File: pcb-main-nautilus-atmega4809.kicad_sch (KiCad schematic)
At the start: 0 parts

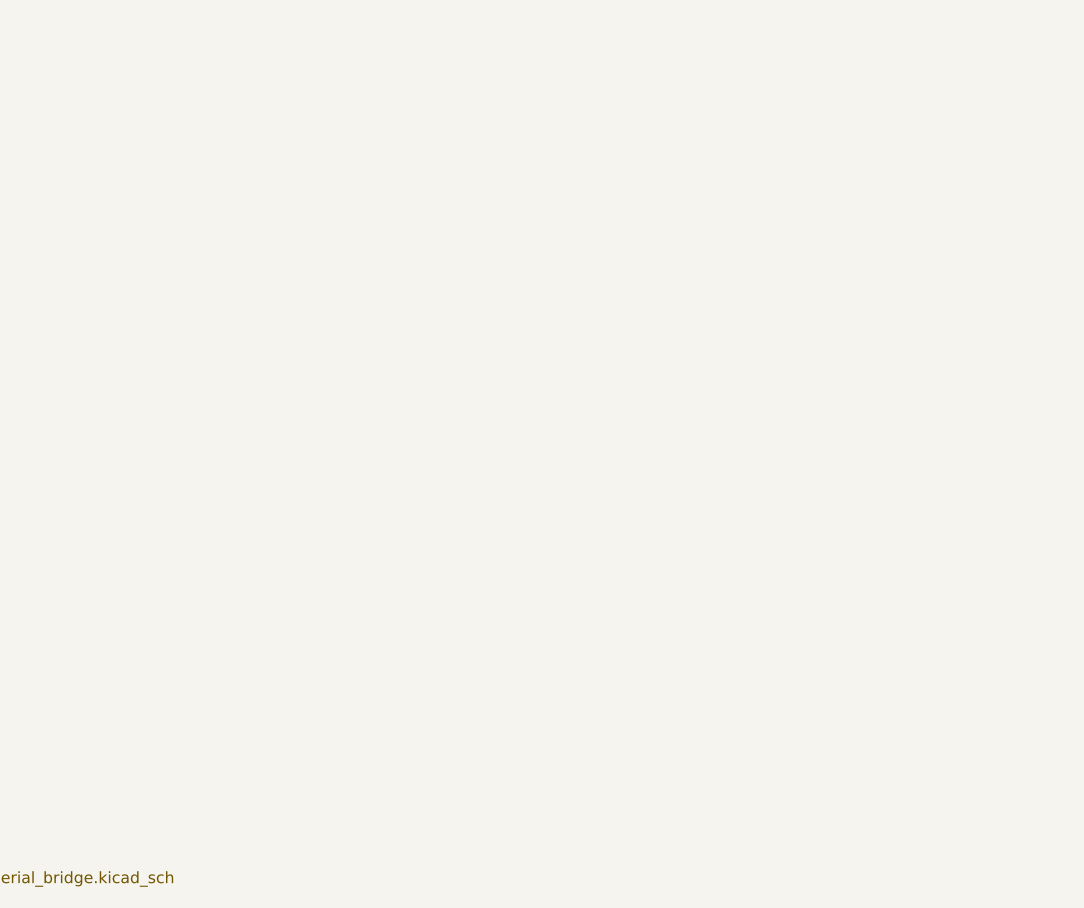
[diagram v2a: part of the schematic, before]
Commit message: Add bi-directional level shifter sheet
Supports #2.
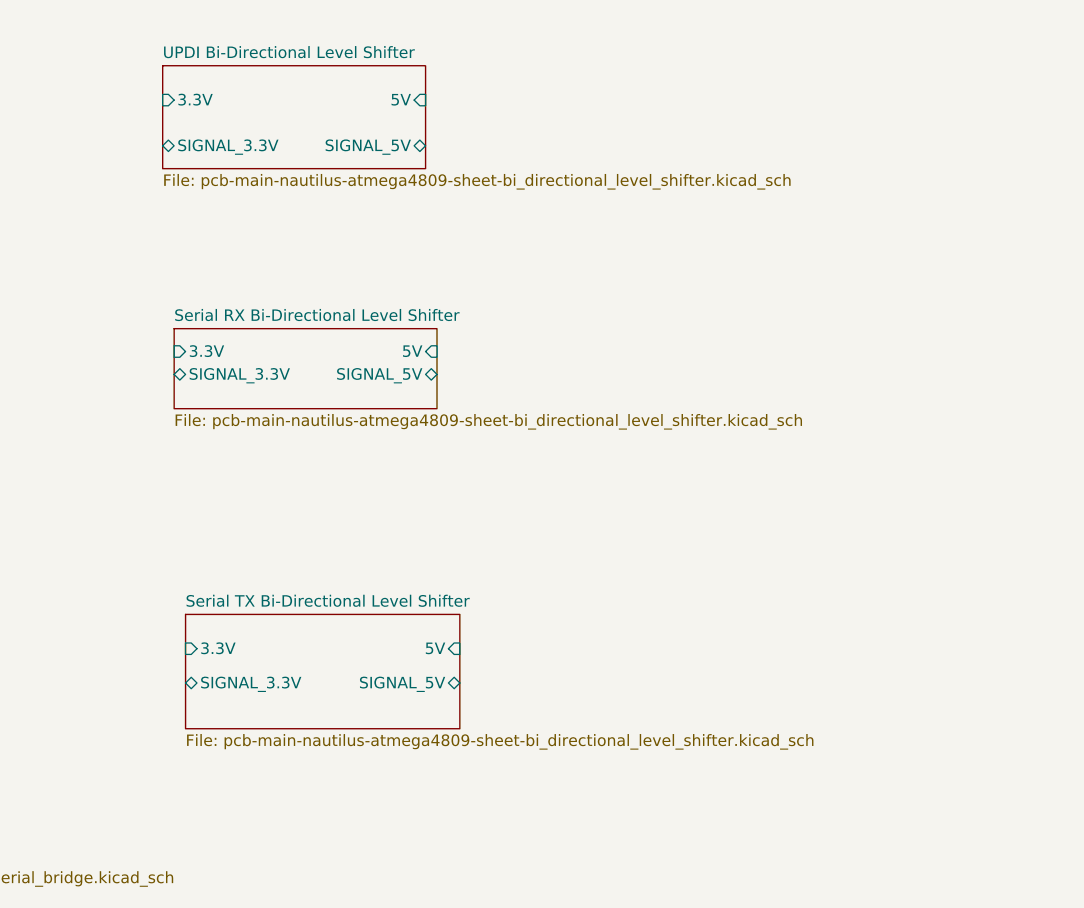
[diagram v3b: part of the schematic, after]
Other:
- added sheet Serial RX Bi-Directional Level Shifter (pcb-main-nautilus-atmega4809-sheet-bi_directional_level_shifter.kicad_sch)
- added sheet Serial TX Bi-Directional Level Shifter (pcb-main-nautilus-atmega4809-sheet-bi_directional_level_shifter.kicad_sch)
- added sheet UPDI Bi-Directional Level Shifter (pcb-main-nautilus-atmega4809-sheet-bi_directional_level_shifter.kicad_sch)
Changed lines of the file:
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@@
     (comment 1 "Derivative of the \"Arduino UNO Rev3\" (https://docs.arduino.cc/hardware/uno-rev3) and\\n\"Arduino Nano Every\" (https://docs.arduino.cc/hardware/nano-every) reference designs")
   )
+  (sheet (at 157.48 40.64) (size 29.21 11.43) (fields_autoplaced)
+    (stroke (width 0.1524) (type solid) (color 0 0 0 0))
+    (fill (color 0 0 0 0.0000))
+    (property "Sheet name" "UPDI Bi-Directional Level Shifter" (id 0) (at 157.48 39.9284 0)
+      (effects (font (size 1.27 1.27)) (justify left bottom))
+    )
+    (property "Sheet file" "pcb-main-nautilus-atmega4809-sheet-bi_directional_level_shifter.kicad_sch" (id 1) (at 157.48 52.6546 0)
+      (effects (font (size 1.27 1.27)) (justify left top))
+    )
+    (pin "5V" input (at 186.69 44.45 0)
+      (effects (font (size 1.27 1.27)) (justify right))
+    )
+    (pin "SIGNAL_5V" bidirectional (at 186.69 49.53 0)
+      (effects (font (size 1.27 1.27)) (justify right))
+    )
+    (pin "3.3V" input (at 157.48 44.45 180)
+      (effects (font (size 1.27 1.27)) (justify left))
+    )
+    (pin "SIGNAL_3.3V" bidirectional (at 157.48 49.53 180)
+      (effects (font (size 1.27 1.27)) (justify left))
+    )
+  )
   (sheet (at 76.2 38.1) (size 20.32 20.32) (fields_autoplaced)
     (stroke (width 0.1524) (type solid) (color 0 0 0 0))
@@
     (pin "UPDI" bidirectional (at 106.68 106.68 0)
       (effects (font (size 1.27 1.27)) (justify right))
+    )
+  )
+  (sheet (at 160.02 101.6) (size 30.48 12.7) (fields_autoplaced)
+    (stroke (width 0.1524) (type solid) (color 0 0 0 0))
+    (fill (color 0 0 0 0.0000))
+    (property "Sheet name" "Serial TX Bi-Directional Level Shifter" (id 0) (at 160.02 100.8884 0)
+      (effects (font (size 1.27 1.27)) (justify left bottom))
+    )
+    (property "Sheet file" "pcb-main-nautilus-atmega4809-sheet-bi_directional_level_shifter.kicad_sch" (id 1) (at 160.02 114.8846 0)
+      (effects (font (size 1.27 1.27)) (justify left top))
+    )
+    (pin "5V" input (at 190.5 105.41 0)
+      (effects (font (size 1.27 1.27)) (justify right))
+    )
+    (pin "SIGNAL_5V" bidirectional (at 190.5 109.22 0)
+      (effects (font (size 1.27 1.27)) (justify right))
+    )
+    (pin "3.3V" input (at 160.02 105.41 180)
+      (effects (font (size 1.27 1.27)) (justify left))
+    )
+    (pin "SIGNAL_3.3V" bidirectional (at 160.02 109.22 180)
+      (effects (font (size 1.27 1.27)) (justify left))
+    )
+  )
+  (sheet (at 158.75 69.85) (size 29.21 8.89) (fields_autoplaced)
+    (stroke (width 0.1524) (type solid) (color 0 0 0 0))
+    (fill (color 0 0 0 0.0000))
+    (property "Sheet name" "Serial RX Bi-Directional Level Shifter" (id 0) (at 158.75 69.1384 0)
+      (effects (font (size 1.27 1.27)) (justify left bottom))
+    )
+    (property "Sheet file" "pcb-main-nautilus-atmega4809-sheet-bi_directional_level_shifter.kicad_sch" (id 1) (at 158.75 79.3246 0)
+      (effects (font (size 1.27 1.27)) (justify left top))
+    )
+    (pin "5V" input (at 187.96 72.39 0)
+      (effects (font (size 1.27 1.27)) (justify right))
+    )
+    (pin "SIGNAL_5V" bidirectional (at 187.96 74.93 0)
+      (effects (font (size 1.27 1.27)) (justify right))
+    )
+    (pin "3.3V" input (at 158.75 72.39 180)
+      (effects (font (size 1.27 1.27)) (justify left))
+    )
+    (pin "SIGNAL_3.3V" bidirectional (at 158.75 74.93 180)
+      (effects (font (size 1.27 1.27)) (justify left))
     )
   )
@@
     (path "/5a33ba3c-72f7-420a-981d-98ac038c5559" (page "2"))
     (path "/9563730f-8d1a-4fdb-af84-834004e725da" (page "3"))
+    (path "/2696b8cf-0d11-49f9-8de6-4c9d32a16799" (page "4"))
+    (path "/b9953305-206e-463a-87bb-3c268da92256" (page "5"))
+    (path "/b67adff0-b650-44cc-9343-28972961f0fd" (page "6"))
   )
   (symbol_instances
@@
       (reference "NT1") (unit 1) (value "NetTie_3") (footprint "")
     )
+    (path "/2696b8cf-0d11-49f9-8de6-4c9d32a16799/faa0bcb3-92cf-49f0-8c93-d9591933f632"
+      (reference "Q1") (unit 1) (value "BSS138PW,115") (footprint "Package_TO_SOT_SMD:SOT-323_SC-70_Handsoldering")
+    )
+    (path "/b9953305-206e-463a-87bb-3c268da92256/faa0bcb3-92cf-49f0-8c93-d9591933f632"
+      (reference "Q2") (unit 1) (value "BSS138PW,115") (footprint "Package_TO_SOT_SMD:SOT-323_SC-70_Handsoldering")
+    )
+    (path "/b67adff0-b650-44cc-9343-28972961f0fd/faa0bcb3-92cf-49f0-8c93-d9591933f632"
+      (reference "Q3") (unit 1) (value "BSS138PW,115") (footprint "Package_TO_SOT_SMD:SOT-323_SC-70_Handsoldering")
+    )
     (path "/5a33ba3c-72f7-420a-981d-98ac038c5559/3e98dc00-be45-4498-ad45-de614d277a00"
       (reference "R1") (unit 1) (value "330/0.1W") (footprint "Resistor_SMD:R_0603_1608Metric_Pad0.98x0.95mm_HandSolder")
@@
       (reference "R4") (unit 1) (value "4.7k/0.1W") (footprint "Resistor_SMD:R_0603_1608Metric_Pad0.98x0.95mm_HandSolder")
     )
+    (path "/2696b8cf-0d11-49f9-8de6-4c9d32a16799/ac494291-0341-40e4-84fe-a220d54d9e87"
+      (reference "R5") (unit 1) (value "4.7k/0.1W") (footprint "Resistor_SMD:R_0603_1608Metric_Pad0.98x0.95mm_HandSolder")
+    )
+    (path "/2696b8cf-0d11-49f9-8de6-4c9d32a16799/08011bfc-ec9f-46b5-8bcb-363c7a858e08"
+      (reference "R6") (unit 1) (value "4.7k/0.1W") (footprint "Resistor_SMD:R_0603_1608Metric_Pad0.98x0.95mm_HandSolder")
+    )
+    (path "/b9953305-206e-463a-87bb-3c268da92256/ac494291-0341-40e4-84fe-a220d54d9e87"
+      (reference "R7") (unit 1) (value "4.7k/0.1W") (footprint "Resistor_SMD:R_0603_1608Metric_Pad0.98x0.95mm_HandSolder")
+    )
+    (path "/b9953305-206e-463a-87bb-3c268da92256/08011bfc-ec9f-46b5-8bcb-363c7a858e08"
+      (reference "R8") (unit 1) (value "4.7k/0.1W") (footprint "Resistor_SMD:R_0603_1608Metric_Pad0.98x0.95mm_HandSolder")
+    )
+    (path "/b67adff0-b650-44cc-9343-28972961f0fd/ac494291-0341-40e4-84fe-a220d54d9e87"
+      (reference "R9") (unit 1) (value "4.7k/0.1W") (footprint "Resistor_SMD:R_0603_1608Metric_Pad0.98x0.95mm_HandSolder")
+    )
+    (path "/b67adff0-b650-44cc-9343-28972961f0fd/08011bfc-ec9f-46b5-8bcb-363c7a858e08"
+      (reference "R10") (unit 1) (value "4.7k/0.1W") (footprint "Resistor_SMD:R_0603_1608Metric_Pad0.98x0.95mm_HandSolder")
+    )
     (path "/5a33ba3c-72f7-420a-981d-98ac038c5559/678f9d4d-d6a2-4e0c-8b54-d5be33abe55a"

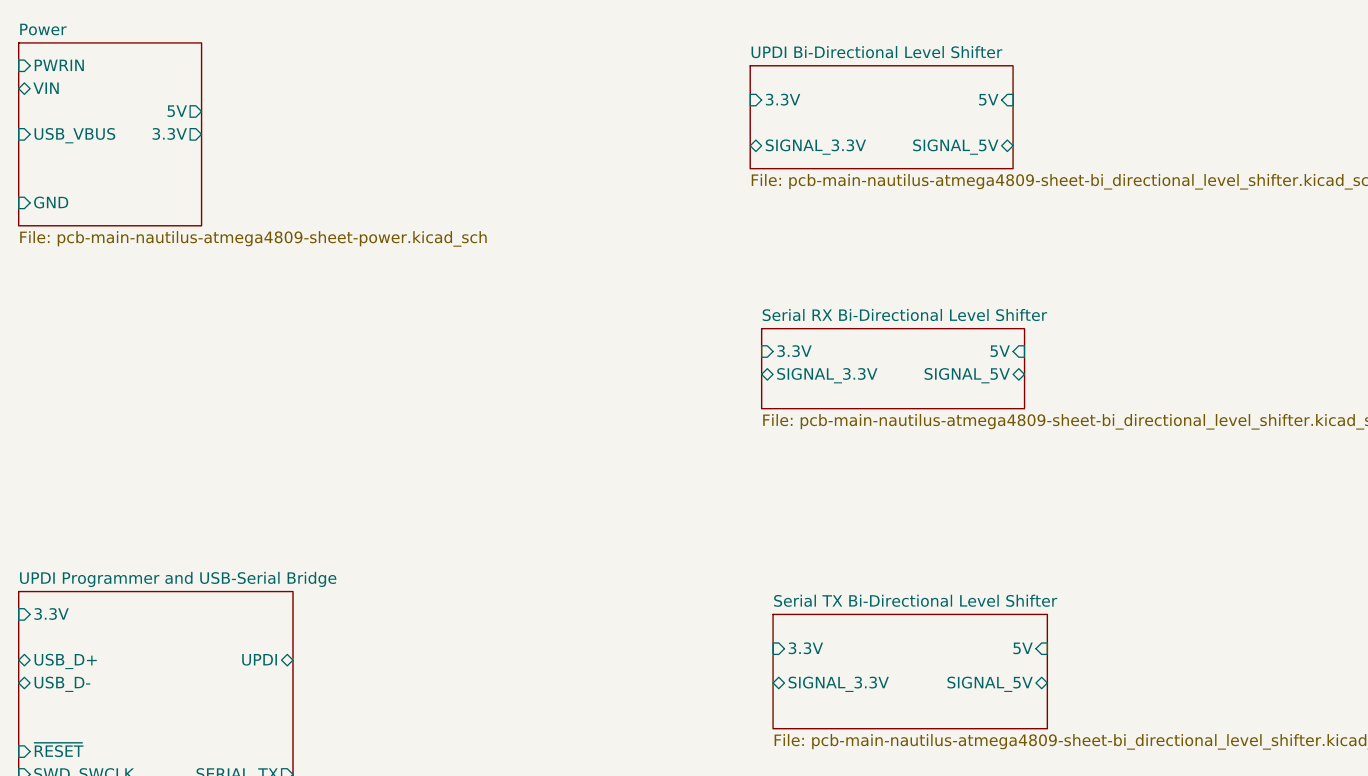
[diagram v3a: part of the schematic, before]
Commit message: Capitalize sheet names
Supports #2.
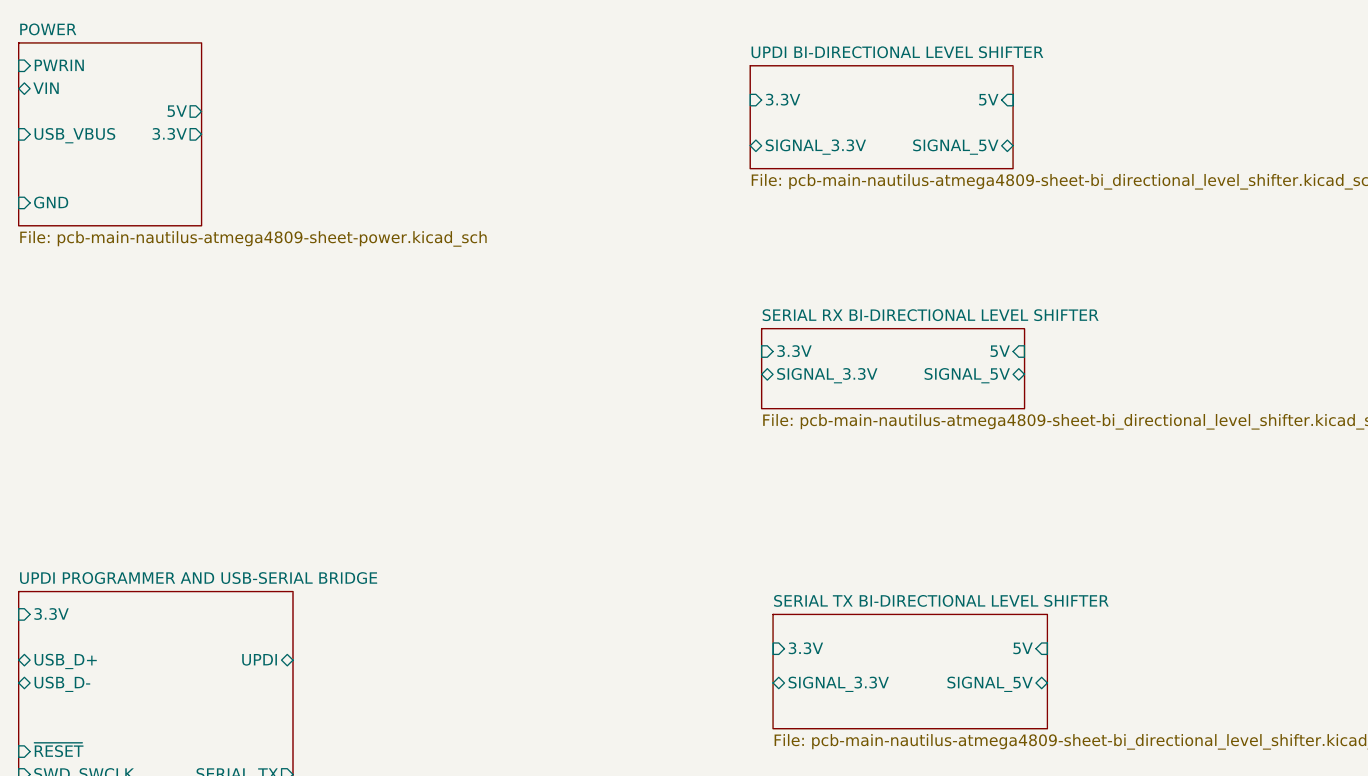
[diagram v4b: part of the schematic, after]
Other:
- sheet Power renamed POWER
- sheet Serial RX Bi-Directional Level Shifter renamed SERIAL RX BI-DIRECTIONAL LEVEL SHIFTER
- sheet Serial TX Bi-Directional Level Shifter renamed SERIAL TX BI-DIRECTIONAL LEVEL SHIFTER
- sheet UPDI Bi-Directional Level Shifter renamed UPDI BI-DIRECTIONAL LEVEL SHIFTER
- sheet UPDI Programmer and USB-Serial Bridge renamed UPDI PROGRAMMER AND USB-SERIAL BRIDGE
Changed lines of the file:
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@@
     (stroke (width 0.1524) (type solid) (color 0 0 0 0))
     (fill (color 0 0 0 0.0000))
-    (property "Sheet name" "UPDI Bi-Directional Level Shifter" (id 0) (at 157.48 39.9284 0)
+    (property "Sheet name" "UPDI BI-DIRECTIONAL LEVEL SHIFTER" (id 0) (at 157.48 39.9284 0)
       (effects (font (size 1.27 1.27)) (justify left bottom))
     )
@@
     (stroke (width 0.1524) (type solid) (color 0 0 0 0))
     (fill (color 0 0 0 0.0000))
-    (property "Sheet name" "Power" (id 0) (at 76.2 37.3884 0)
+    (property "Sheet name" "POWER" (id 0) (at 76.2 37.3884 0)
       (effects (font (size 1.27 1.27)) (justify left bottom))
     )
@@
     (stroke (width 0.1524) (type solid) (color 0 0 0 0))
     (fill (color 0 0 0 0.0000))
-    (property "Sheet name" "UPDI Programmer and USB-Serial Bridge" (id 0) (at 76.2 98.3484 0)
+    (property "Sheet name" "UPDI PROGRAMMER AND USB-SERIAL BRIDGE" (id 0) (at 76.2 98.3484 0)
       (effects (font (size 1.27 1.27)) (justify left bottom))
     )
@@
     (stroke (width 0.1524) (type solid) (color 0 0 0 0))
     (fill (color 0 0 0 0.0000))
-    (property "Sheet name" "Serial TX Bi-Directional Level Shifter" (id 0) (at 160.02 100.8884 0)
+    (property "Sheet name" "SERIAL TX BI-DIRECTIONAL LEVEL SHIFTER" (id 0) (at 160.02 100.8884 0)
       (effects (font (size 1.27 1.27)) (justify left bottom))
     )
@@
     (stroke (width 0.1524) (type solid) (color 0 0 0 0))
     (fill (color 0 0 0 0.0000))
-    (property "Sheet name" "Serial RX Bi-Directional Level Shifter" (id 0) (at 158.75 69.1384 0)
+    (property "Sheet name" "SERIAL RX BI-DIRECTIONAL LEVEL SHIFTER" (id 0) (at 158.75 69.1384 0)
       (effects (font (size 1.27 1.27)) (justify left bottom))
     )
